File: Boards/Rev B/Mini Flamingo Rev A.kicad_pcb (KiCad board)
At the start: 2 copper layers, 37.5 x 24.4 mm, 23 parts, among them J1 ISP_Header, J2 APA102C Out, J3 Batt Conn, SW1 Power Switch, U1 ATTINY85-20SU, U2 APA102C

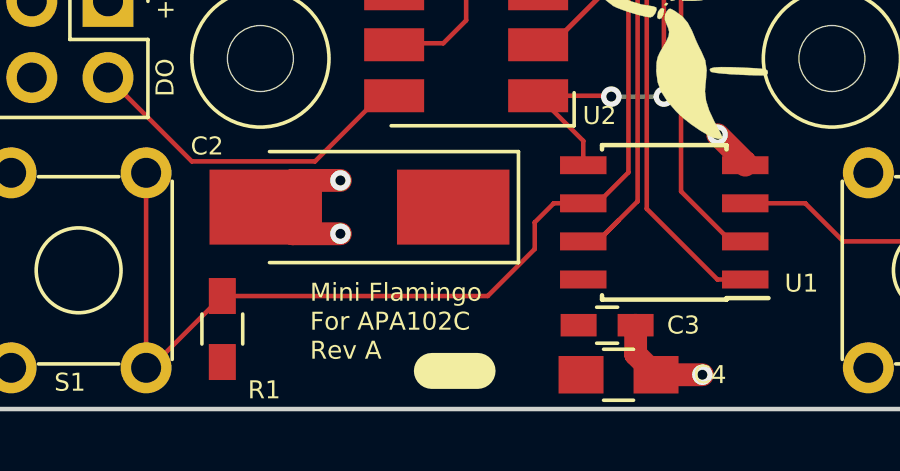
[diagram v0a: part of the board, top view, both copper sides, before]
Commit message: First Rev A test code and added Rev A blue wire to Rev B
There were two +BAT pours that were not connected. They are now
connected with a via.

The forum suggests removing C1; I will consider this for Rev B.
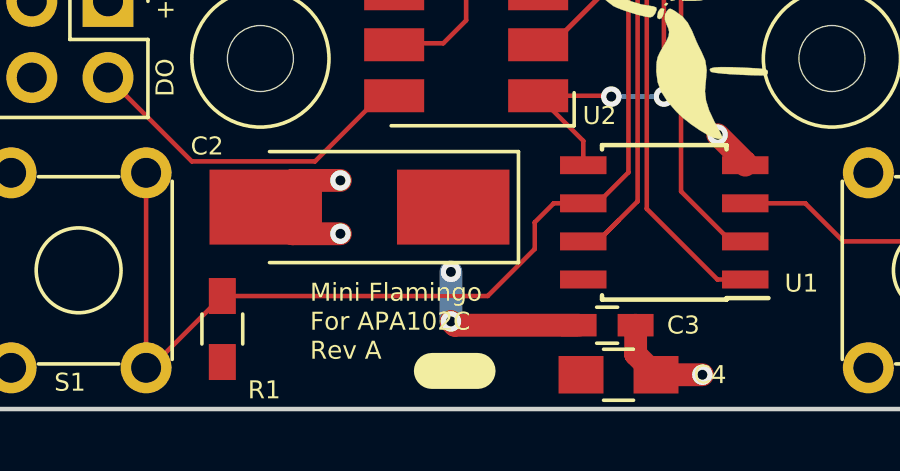
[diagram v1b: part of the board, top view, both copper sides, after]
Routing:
- net +BATT: track 15.5 -> 21.5 mm, vias 10 -> 12
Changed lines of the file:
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@@
 (kicad_pcb (version 4) (host pcbnew 4.0.7)
   (general
-    (links 0)
+    (links 50)
     (no_connects 1)
-    (area 150.419999 74.219999 188.035001 98.754001)
+    (area 149.1762 73.5962 188.8428 100.0188)
     (thickness 1.6)
     (drawings 29)
-    (tracks 152)
+    (tracks 157)
     (zones 0)
     (modules 23)
@@
   (page A4)
   (layers
-    (0 F.Cu signal hide)
-    (31 B.Cu signal hide)
+    (0 F.Cu signal)
+    (31 B.Cu signal)
     (32 B.Adhes user)
     (33 F.Adhes user)
@@
     (effects (font (size 0.6 0.6) (thickness 0.15)) (justify left))
   )
-  (gr_text "Mini Flamingo\nFor APA102C\nRev A" (at 162.941 95.758 360) (layer F.SilkS)
+  (gr_text "Mini Flamingo\nFor APA102C\nRev A" (at 162.941 95.758) (layer F.SilkS)
     (effects (font (size 0.6 0.6) (thickness 0.15)) (justify left))
   )
@@
   (segment (start 170.548 84.836) (end 171.069 84.836) (width 0.762) (layer F.Cu) (net 2))
   (segment (start 161.467 91.948) (end 160.528 91.948) (width 0.762) (layer F.Cu) (net 2))
+  (segment (start 167.64 95.758) (end 167.64 94.107) (width 0.762) (layer B.Cu) (net 3))
+  (via (at 167.64 94.107) (size 0.6858) (drill 0.3302) (layers F.Cu B.Cu) (net 3))
+  (segment (start 171.897 95.885) (end 167.767 95.885) (width 0.762) (layer F.Cu) (net 3))
+  (segment (start 167.767 95.885) (end 167.64 95.758) (width 0.762) (layer F.Cu) (net 3))
+  (via (at 167.64 95.758) (size 0.6858) (drill 0.3302) (layers F.Cu B.Cu) (net 3))
   (segment (start 157.988 83.566) (end 157.988 82.296) (width 1.27) (layer B.Cu) (net 3))
   (segment (start 158.877 83.566) (end 158.877 82.296) (width 1.27) (layer B.Cu) (net 3))
